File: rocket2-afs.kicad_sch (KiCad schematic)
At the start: 64 parts, among them J1 ARMING_PLUG, J2 POWER, J3 E-MATCH_DROGUE, J4 SWD, J5 E-MATCH_RECOVERY, Q1 Q_NMOS_GSD, Q2 Q_NMOS_GSD, Q3 Q_NMOS_GSD, Q4 Q_NMOS_GSD, Q5 Q_NMOS_GSD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

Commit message: Complete PCB, first iteration
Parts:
- BZ1: footprint UCIRP-KiCAD-Lib:CUI_CMI-9653S-SMT -> Buzzer_Beeper:Buzzer_CUI_CPT-9019S-SMT
- J2: footprint (none) -> TerminalBlock:TerminalBlock_bornier-2_P5.08mm
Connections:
- net BUZZER_PWM: now also U1.55 (PB3); no longer U1.14 (PA0)
- net USB_DM renamed USB_CONN_D-
- net USB_CONN_D-: now also J6.A7 (D-), J6.B7 (D-); no longer U1.44 (PA11)
- removed net USB_DM_CON: J6.A7 (D-), J6.B7 (D-), U8.6 (I/O1)
- net USB_DP renamed USB_CONN_D+
- net USB_CONN_D+: now also J6.A6 (D+), J6.B6 (D+); no longer U1.45 (PA12)
- removed net USB_DP_CON: J6.A6 (D+), J6.B6 (D+), U8.4 (I/O2)
- new net USB_D+: U1.45 (PA12), U8.4 (I/O2)
- new net USB_D-: U1.44 (PA11), U8.6 (I/O1)
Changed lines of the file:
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@@
   (no_connect (at 173.99 96.52))
   (no_connect (at 173.99 119.38))
-  (no_connect (at 78.74 64.77))
   (no_connect (at 173.99 113.03))
   (no_connect (at 78.74 101.6))
@@
   (no_connect (at 199.39 104.14))
   (no_connect (at 78.74 87.63))
+  (no_connect (at 33.02 57.15))
   (no_connect (at 124.46 153.67))
   (no_connect (at 199.39 106.68))
@@
     )
   )
+  (global_label "USB_CONN_D-" (shape input) (at 172.72 90.17 180) (fields_autoplaced)
+    (effects (font (size 1.27 1.27)) (justify right))
+    (property "Intersheetrefs" "${INTERSHEET_REFS}" (at 155.8857 90.17 0)
+      (effects (font (size 1.27 1.27)) (justify right) hide)
+    )
+  )
   (global_label "GPS_SAFEBOOT" (shape input) (at 203.2 48.26 0) (fields_autoplaced)
     (effects (font (size 1.27 1.27)) (justify left))
@@
     )
   )
-  (global_label "USB_DP_CON" (shape input) (at 172.72 85.09 180) (fields_autoplaced)
-    (effects (font (size 1.27 1.27)) (justify right))
-    (property "Intersheetrefs" "${INTERSHEET_REFS}" (at 157.5186 85.09 0)
-      (effects (font (size 1.27 1.27)) (justify right) hide)
-    )
-  )
   (global_label "DROGUE_CONT" (shape input) (at 33.02 99.06 180) (fields_autoplaced)
     (effects (font (size 1.27 1.27)) (justify right))
@@
     )
   )
-  (global_label "BUZZER_PWM" (shape input) (at 33.02 57.15 180) (fields_autoplaced)
-    (effects (font (size 1.27 1.27)) (justify right))
-    (property "Intersheetrefs" "${INTERSHEET_REFS}" (at 17.4559 57.15 0)
-      (effects (font (size 1.27 1.27)) (justify right) hide)
+  (global_label "BUZZER_PWM" (shape input) (at 78.74 64.77 0) (fields_autoplaced)
+    (effects (font (size 1.27 1.27)) (justify left))
+    (property "Intersheetrefs" "${INTERSHEET_REFS}" (at 94.3041 64.77 0)
+      (effects (font (size 1.27 1.27)) (justify left) hide)
     )
   )
@@
     )
   )
-  (global_label "USB_DM_CON" (shape input) (at 172.72 90.17 180) (fields_autoplaced)
-    (effects (font (size 1.27 1.27)) (justify right))
-    (property "Intersheetrefs" "${INTERSHEET_REFS}" (at 157.3372 90.17 0)
-      (effects (font (size 1.27 1.27)) (justify right) hide)
-    )
-  )
   (global_label "GPS_SCL" (shape input) (at 158.75 45.72 180) (fields_autoplaced)
     (effects (font (size 1.27 1.27)) (justify right))
@@
     )
   )
+  (global_label "USB_D-" (shape input) (at 33.02 85.09 180) (fields_autoplaced)
+    (effects (font (size 1.27 1.27)) (justify right))
+    (property "Intersheetrefs" "${INTERSHEET_REFS}" (at 22.4148 85.09 0)
+      (effects (font (size 1.27 1.27)) (justify right) hide)
+    )
+  )
   (global_label "GPS_SDA" (shape input) (at 158.75 48.26 180) (fields_autoplaced)
     (effects (font (size 1.27 1.27)) (justify right))
@@
     )
   )
-  (global_label "USB_DP_CON" (shape input) (at 326.39 40.64 0) (fields_autoplaced)
-    (effects (font (size 1.27 1.27)) (justify left))
-    (property "Intersheetrefs" "${INTERSHEET_REFS}" (at 341.5914 40.64 0)
+  (global_label "USB_CONN_D+" (shape input) (at 326.39 45.72 0) (fields_autoplaced)
+    (effects (font (size 1.27 1.27)) (justify left))
+    (property "Intersheetrefs" "${INTERSHEET_REFS}" (at 343.2243 45.72 0)
       (effects (font (size 1.27 1.27)) (justify left) hide)
     )
@@
     )
   )
-  (global_label "USB_DP" (shape input) (at 326.39 45.72 0) (fields_autoplaced)
-    (effects (font (size 1.27 1.27)) (justify left))
-    (property "Intersheetrefs" "${INTERSHEET_REFS}" (at 336.6928 45.72 0)
+  (global_label "USB_D+" (shape input) (at 326.39 40.64 0) (fields_autoplaced)
+    (effects (font (size 1.27 1.27)) (justify left))
+    (property "Intersheetrefs" "${INTERSHEET_REFS}" (at 336.9952 40.64 0)
       (effects (font (size 1.27 1.27)) (justify left) hide)
     )
@@
     )
   )
-  (global_label "USB_DM" (shape input) (at 33.02 85.09 180) (fields_autoplaced)
-    (effects (font (size 1.27 1.27)) (justify right))
-    (property "Intersheetrefs" "${INTERSHEET_REFS}" (at 22.5358 85.09 0)
-      (effects (font (size 1.27 1.27)) (justify right) hide)
-    )
-  )
-  (global_label "USB_DM" (shape input) (at 306.07 45.72 180) (fields_autoplaced)
-    (effects (font (size 1.27 1.27)) (justify right))
-    (property "Intersheetrefs" "${INTERSHEET_REFS}" (at 295.5858 45.72 0)
-      (effects (font (size 1.27 1.27)) (justify right) hide)
-    )
-  )
-  (global_label "USB_DM_CON" (shape input) (at 306.07 40.64 180) (fields_autoplaced)
-    (effects (font (size 1.27 1.27)) (justify right))
-    (property "Intersheetrefs" "${INTERSHEET_REFS}" (at 290.6872 40.64 0)
-      (effects (font (size 1.27 1.27)) (justify right) hide)
-    )
-  )
-  (global_label "USB_DP" (shape input) (at 33.02 87.63 180) (fields_autoplaced)
-    (effects (font (size 1.27 1.27)) (justify right))
-    (property "Intersheetrefs" "${INTERSHEET_REFS}" (at 22.7172 87.63 0)
+  (global_label "USB_D-" (shape input) (at 306.07 40.64 180) (fields_autoplaced)
+    (effects (font (size 1.27 1.27)) (justify right))
+    (property "Intersheetrefs" "${INTERSHEET_REFS}" (at 295.4648 40.64 0)
+      (effects (font (size 1.27 1.27)) (justify right) hide)
+    )
+  )
+  (global_label "USB_CONN_D-" (shape input) (at 306.07 45.72 180) (fields_autoplaced)
+    (effects (font (size 1.27 1.27)) (justify right))
+    (property "Intersheetrefs" "${INTERSHEET_REFS}" (at 289.2357 45.72 0)
       (effects (font (size 1.27 1.27)) (justify right) hide)
     )
@@
     )
   )
+  (global_label "USB_D+" (shape input) (at 33.02 87.63 180) (fields_autoplaced)
+    (effects (font (size 1.27 1.27)) (justify right))
+    (property "Intersheetrefs" "${INTERSHEET_REFS}" (at 22.4148 87.63 0)
+      (effects (font (size 1.27 1.27)) (justify right) hide)
+    )
+  )
   (global_label "IMU_INT1" (shape input) (at 267.97 49.53 0) (fields_autoplaced)
     (effects (font (size 1.27 1.27)) (justify left))
@@
     (effects (font (size 1.27 1.27)) (justify right))
     (property "Intersheetrefs" "${INTERSHEET_REFS}" (at 22.2334 69.85 0)
+      (effects (font (size 1.27 1.27)) (justify right) hide)
+    )
+  )
+  (global_label "USB_CONN_D+" (shape input) (at 172.72 85.09 180) (fields_autoplaced)
+    (effects (font (size 1.27 1.27)) (justify right))
+    (property "Intersheetrefs" "${INTERSHEET_REFS}" (at 155.8857 85.09 0)
       (effects (font (size 1.27 1.27)) (justify right) hide)
     )
@@
       (effects (font (size 1.27 1.27)) (justify left))
     )
-    (property "Footprint" "UCIRP-KiCAD-Lib:CUI_CMI-9653S-SMT" (at 130.175 71.12 90)
+    (property "Footprint" "Buzzer_Beeper:Buzzer_CUI_CPT-9019S-SMT" (at 130.175 71.12 90)
       (effects (font (size 1.27 1.27)) hide)
     )
@@
       (effects (font (size 1.27 1.27)))
     )
-    (property "Footprint" "" (at 30.48 177.8 0)
-      (effects (font (size 1.27 1.27)) hide)
-    )
+    (property "Footprint" "TerminalBlock:TerminalBlock_bornier-2_P5.08mm" (at 30.48 177.8 0)
+      (effects (font (size 1.27 1.27)) hide)
+    )

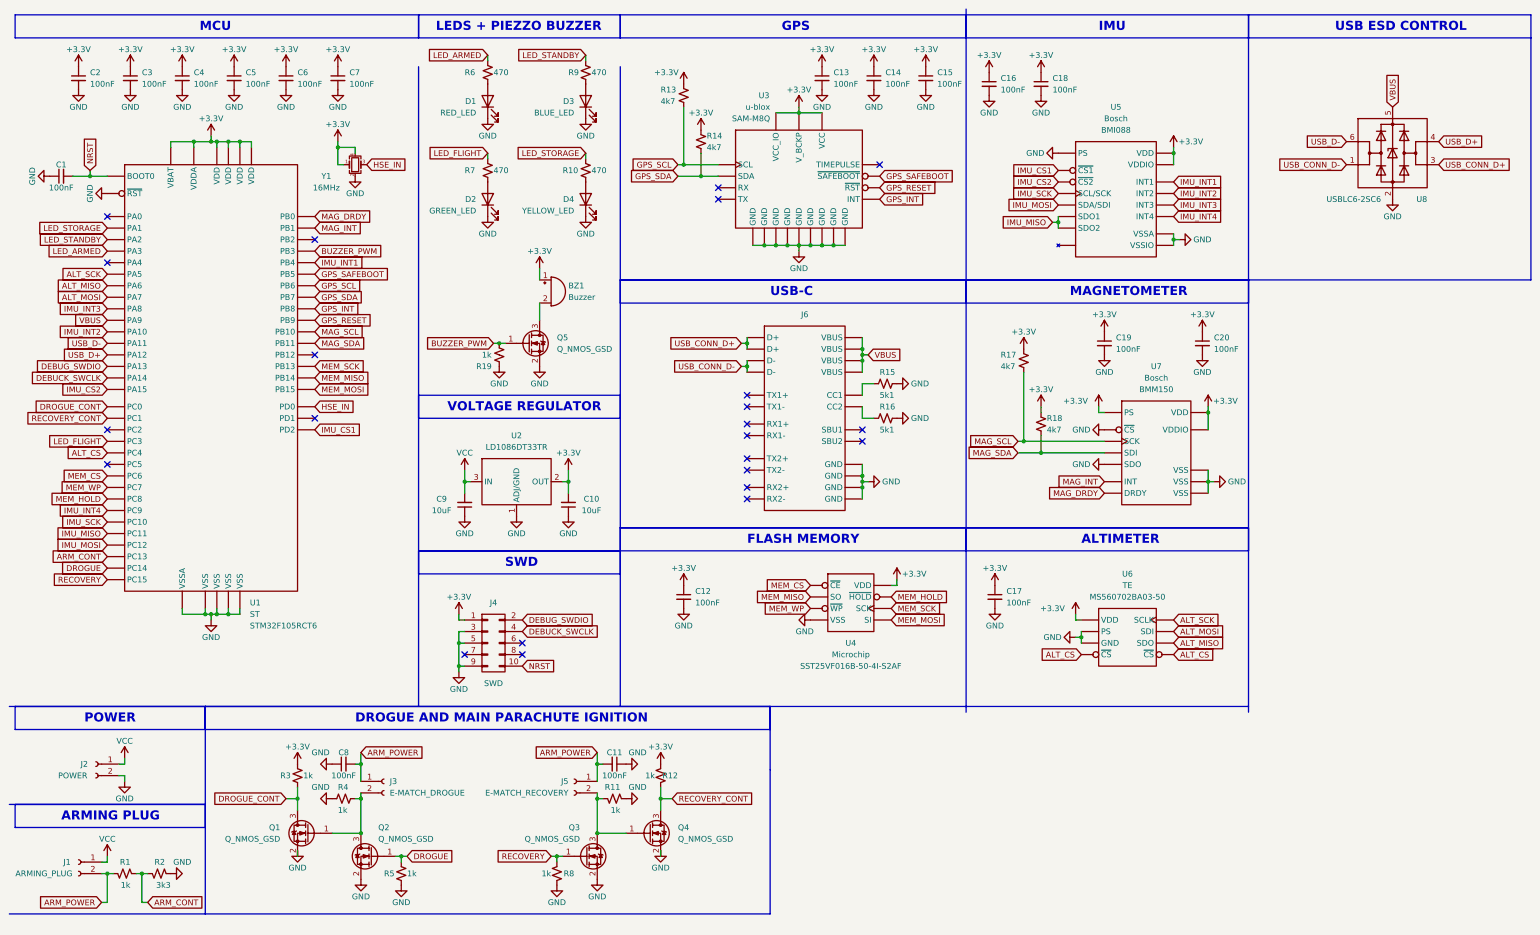
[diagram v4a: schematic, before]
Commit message: Current limiting resistors to MOSFETs. Silkscreen names + Logo. Adjusted BMI088 footprint as per ERC error (LOCAL TO PCB).
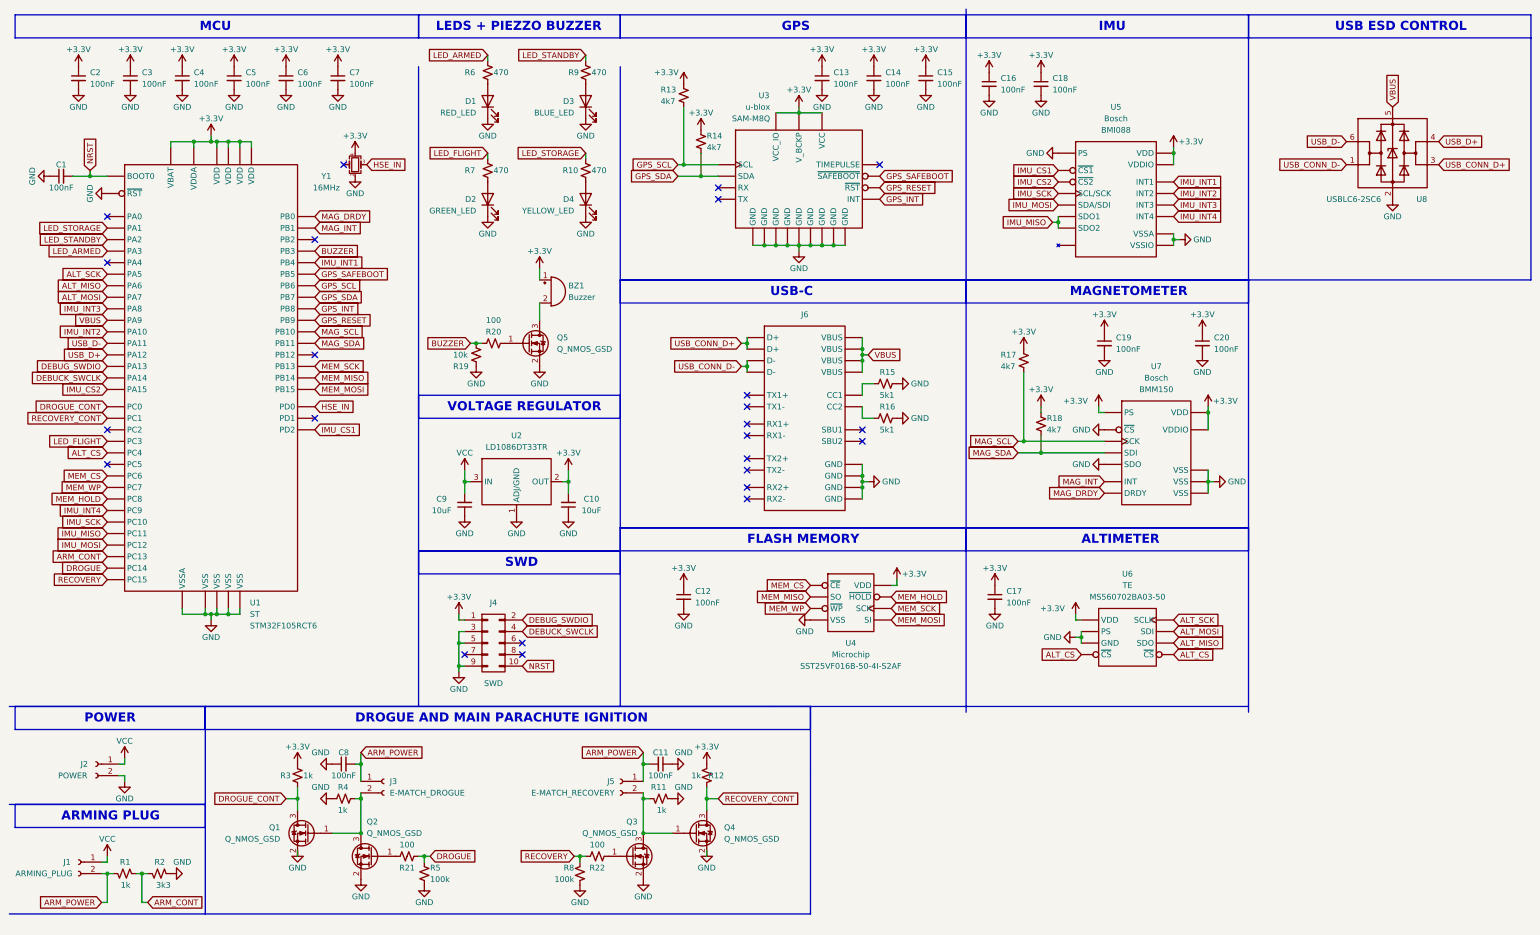
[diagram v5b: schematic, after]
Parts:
- added R20, R21, R22: 100, Resistor_SMD:R_0603_1608Metric, symbol Device:R_Small_US
- R19: value 1k -> 10k
- R5, R8: value 1k -> 100k
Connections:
- net +3.3V: no longer Y1.1
- net DROGUE: now also R21.2; no longer Q2.1 (G)
- net RECOVERY: now also R22.1; no longer Q3.1 (G)
- net BUZZER_PWM renamed BUZZER
- net BUZZER: now also R20.1; no longer Q5.1 (G)
- new net: Q3.1 (G), R22.2
- new net: Q5.1 (G), R20.2
- new net: Q2.1 (G), R21.1
- no-connect marks 23 -> 24
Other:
- moved on the sheet: C11, J5, Q3, Q4, R11, R12, R19, R5, R8

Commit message: wrote in comments
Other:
- note added: "*IMPORTANT*"
- note added: "PCB Considerations (PAGE 12)"
- note added: "REF (PG 11)"
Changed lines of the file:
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@@
     (fill (type color) (color 20 0 205 0.11))
+  )
+  (text_box "increase to 10k"
+    (at 82.55 188.595 0) (size 5.08 2.54)
+    (stroke (width 0) (type default))
+    (fill (type none))
+    (effects (font (size 0.7 0.7)) (justify left top))
+  )
+  (text_box "Place on large GND plane (as uninterupted as possible)"
+    (at 148.59 60.325 0) (size 13.335 5.715)
+    (stroke (width 0) (type default))
+    (fill (type none))
+    (effects (font (size 0.8 0.8)) (justify left top))
+  )
+  (text_box "I would leave INT open / NC\n(safer)"
+    (at 203.2 55.88 0) (size 8.255 6.35)
+    (stroke (width 0) (type default))
+    (fill (type none))
+    (effects (font (size 0.8 0.8)) (justify left top))
+  )
+  (text_box "increase to 10k"
+    (at 153.035 188.595 0) (size 5.08 2.54)
+    (stroke (width 0) (type default))
+    (fill (type none))
+    (effects (font (size 0.7 0.7)) (justify left top))
+  )
+  (text_box "reduce to 10k"
+    (at 106.68 205.105 0) (size 8.89 5.08)
+    (stroke (width 0) (type default))
+    (fill (type none))
+    (effects (font (size 1.27 1.27)) (justify left top))
+  )
+  (text_box "SDA and SCL have internal pull-ups\n(PAGE 5)"
+    (at 149.86 35.56 0) (size 8.89 6.985)
+    (stroke (width 0) (type default))
+    (fill (type none))
+    (effects (font (size 0.8 0.8)) (justify left top) (href "https://content.u-blox.com/sites/default/files/SAM-M8Q_HardwareIntegrationManual_%28UBX-16018358%29.pdf"))
+  )
+  (text_box "reduce to 10k"
+    (at 125.73 205.105 0) (size 8.89 5.08)
+    (stroke (width 0) (type default))
+    (fill (type none))
+    (effects (font (size 1.27 1.27)) (justify left top))
   )
   (text "POWER" (at 27.94 168.91 0)
@@
   (text "USB ESD CONTROL" (at 303.53 16.51 0)
     (effects (font (size 2 2) (thickness 0.4) bold) (justify left bottom))
+  )
+  (text "PCB Considerations (PAGE 12)" (at 148.59 68.58 0)
+    (effects (font (size 1.27 1.27)) (justify left bottom) (href "https://content.u-blox.com/sites/default/files/SAM-M8Q_HardwareIntegrationManual_%28UBX-16018358%29.pdf"))
   )
   (text "ARMING PLUG" (at 22.86 190.5 0)
@@
   (text "MCU" (at 53.34 16.51 0)
     (effects (font (size 2 2) (thickness 0.4) bold) (justify left bottom))
+  )
+  (text "*IMPORTANT*" (at 163.195 66.04 0)
+    (effects (font (size 0.9 0.9)) (justify left bottom))
   )
   (text "ALTIMETER" (at 247.65 129.54 0)
@@
     (effects (font (size 2 2) (thickness 0.4) bold) (justify left bottom))
   )
+  (text "REF (PG 11)" (at 203.835 64.135 0)
+    (effects (font (size 0.8 0.8)) (justify left bottom) (href "https://content.u-blox.com/sites/default/files/SAM-M8Q_DataSheet_%28UBX-16012619%29.pdf"))
+  )
   (text "VOLTAGE REGULATOR" (at 107.95 100.33 0)
